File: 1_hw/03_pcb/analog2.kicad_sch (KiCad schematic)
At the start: 17 parts

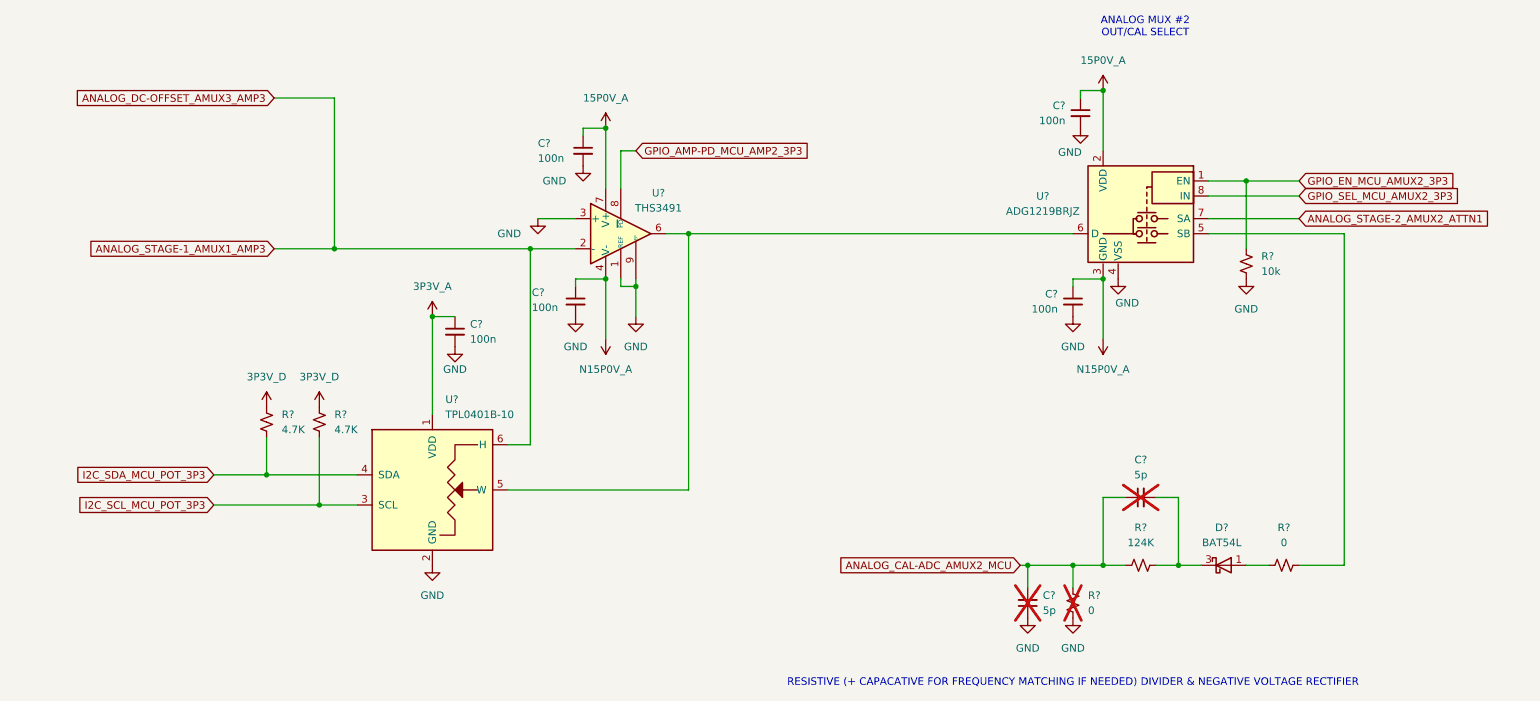
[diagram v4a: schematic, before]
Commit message: FEAT: Added Clocking Sheet, FPGA Flash, and FPGA Decoupling.
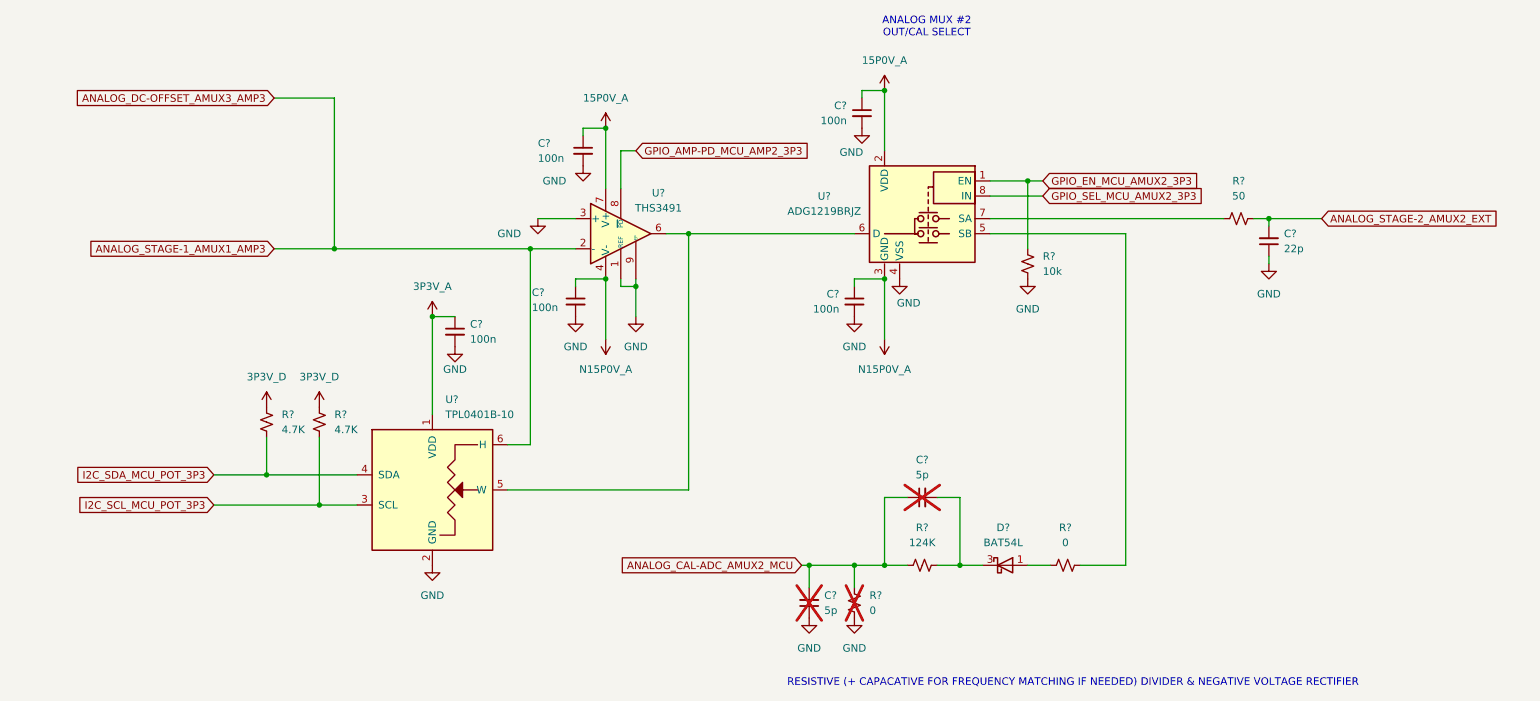
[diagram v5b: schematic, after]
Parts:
- added C?: 22p, symbol Device:C_Small
- added R?: 50, symbol Device:R_Small_US
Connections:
- net GND: now also C?.1
- net ANALOG_STAGE-2_AMUX2_ATTN1: no longer names the net of U?.7 (SA)
- net ANALOG_STAGE-2_AMUX2_ATTN1: now also R?.2
- new net ANALOG_STAGE-2_AMUX2_EXT: C?.2, R?.1
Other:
- moved on the sheet: C?, D?, R?, U?

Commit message: FEAT: Added Connectors on Schematic. Created Connector Footprints.
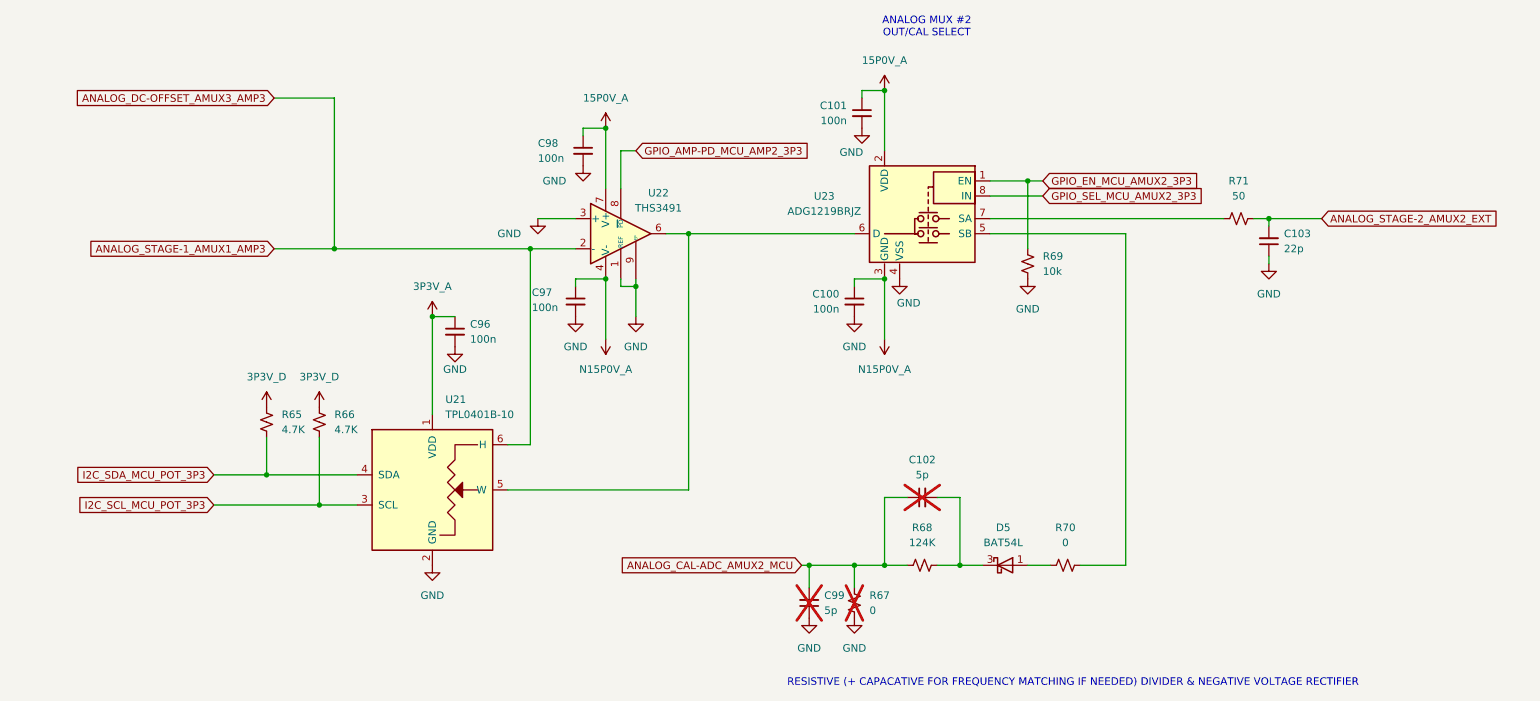
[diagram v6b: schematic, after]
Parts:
- gave numbers to parts that had none: 19
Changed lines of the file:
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@@
 		(dnp no)
 		(fields_autoplaced yes)
-		(property "Reference" "U?"
+		(property "Reference" "U21"
 			(at 83.4741 111.76 0)
 			(effects
@@
 			(project ""
 				(path "/866ef9be-3b01-4288-a6e0-a2357aa17e50/e46c6640-71a3-4b78-b602-0f6be9676e36"
-					(reference "U?")
+					(reference "U21")
 					(unit 1)
 				)
@@
 		(dnp yes)
 		(fields_autoplaced yes)
-		(property "Reference" "R?"
+		(property "Reference" "R67"
 			(at 154.94 144.7799 0)
 			(effects
@@
 			(project "arb"
 				(path "/866ef9be-3b01-4288-a6e0-a2357aa17e50/e46c6640-71a3-4b78-b602-0f6be9676e36"
-					(reference "R?")
+					(reference "R67")
 					(unit 1)
 				)
@@
 		(dnp no)
 		(fields_autoplaced yes)
-		(property "Reference" "R?"
+		(property "Reference" "R69"
 			(at 184.15 87.6299 0)
 			(effects
@@
 			(project "arb"
 				(path "/866ef9be-3b01-4288-a6e0-a2357aa17e50/e46c6640-71a3-4b78-b602-0f6be9676e36"
-					(reference "R?")
+					(reference "R69")
 					(unit 1)
 				)
@@
 		(dnp no)
 		(fields_autoplaced yes)
-		(property "Reference" "C?"
+		(property "Reference" "C101"
 			(at 151.13 62.2363 0)
 			(effects
@@
 			(project "arb"
 				(path "/866ef9be-3b01-4288-a6e0-a2357aa17e50/e46c6640-71a3-4b78-b602-0f6be9676e36"
-					(reference "C?")
+					(reference "C101")
 					(unit 1)
 				)
@@
 		(dnp yes)
 		(fields_autoplaced yes)
-		(property "Reference" "C?"
+		(property "Reference" "C99"
 			(at 147.32 144.7735 0)
 			(effects
@@
 			(project "arb"
 				(path "/866ef9be-3b01-4288-a6e0-a2357aa17e50/e46c6640-71a3-4b78-b602-0f6be9676e36"
-					(reference "C?")
+					(reference "C99")
 					(unit 1)
 				)
@@
 		(on_board yes)
 		(dnp no)
-		(property "Reference" "U?"
+		(property "Reference" "U22"
 			(at 119.38 76.962 0)
 			(effects
@@
 			(project ""
 				(path "/866ef9be-3b01-4288-a6e0-a2357aa17e50/e46c6640-71a3-4b78-b602-0f6be9676e36"
-					(reference "U?")
+					(reference "U22")
 					(unit 1)
 				)
@@
 		(on_board yes)
 		(dnp no)
-		(property "Reference" "C?"
+		(property "Reference" "C98"
 			(at 99.06 68.58 0)
 			(effects
@@
 			(project "arb"
 				(path "/866ef9be-3b01-4288-a6e0-a2357aa17e50/e46c6640-71a3-4b78-b602-0f6be9676e36"
-					(reference "C?")
+					(reference "C98")
 					(unit 1)
 				)
@@
 		(dnp no)
 		(fields_autoplaced yes)
-		(property "Reference" "C?"
+		(property "Reference" "C100"
 			(at 149.86 93.9863 0)
 			(effects
@@
 			(project "arb"
 				(path "/866ef9be-3b01-4288-a6e0-a2357aa17e50/e46c6640-71a3-4b78-b602-0f6be9676e36"
-					(reference "C?")
+					(reference "C100")
 					(unit 1)
 				)
@@
 		(dnp no)
 		(fields_autoplaced yes)
-		(property "Reference" "R?"
+		(property "Reference" "R68"
 			(at 163.83 133.35 90)
 			(effects
@@
 			(project "arb"
 				(path "/866ef9be-3b01-4288-a6e0-a2357aa17e50/e46c6640-71a3-4b78-b602-0f6be9676e36"
-					(reference "R?")
+					(reference "R68")
 					(unit 1)
 				)
@@
 		(on_board yes)
 		(dnp no)
-		(property "Reference" "C?"
+		(property "Reference" "C97"
 			(at 98.044 93.726 0)
 			(effects
@@
 			(project "arb"
 				(path "/866ef9be-3b01-4288-a6e0-a2357aa17e50/e46c6640-71a3-4b78-b602-0f6be9676e36"
-					(reference "C?")
+					(reference "C97")
 					(unit 1)
 				)
@@
 		(dnp no)
 		(fields_autoplaced yes)
-		(property "Reference" "R?"
+		(property "Reference" "R70"
 			(at 187.96 133.35 90)
 			(effects
@@
 			(project "arb"
 				(path "/866ef9be-3b01-4288-a6e0-a2357aa17e50/e46c6640-71a3-4b78-b602-0f6be9676e36"
-					(reference "R?")
+					(reference "R70")
 					(unit 1)
 				)
@@
 		(dnp no)
 		(fields_autoplaced yes)
-		(property "Reference" "R?"
+		(property "Reference" "R66"
 			(at 64.77 114.2999 0)
 			(effects
@@
 			(project "arb"
 				(path "/866ef9be-3b01-4288-a6e0-a2357aa17e50/e46c6640-71a3-4b78-b602-0f6be9676e36"
-					(reference "R?")
+					(reference "R66")
 					(unit 1)
 				)
@@
 		(dnp yes)
 		(fields_autoplaced yes)
-		(property "Reference" "C?"
+		(property "Reference" "C102"
 			(at 163.8363 121.92 90)
 			(effects
@@
 			(project "arb"
 				(path "/866ef9be-3b01-4288-a6e0-a2357aa17e50/e46c6640-71a3-4b78-b602-0f6be9676e36"
-					(reference "C?")
+					(reference "C102")
 					(unit 1)
 				)
@@
 		(dnp no)
 		(fields_autoplaced yes)
-		(property "Reference" "R?"
+		(property "Reference" "R71"
 			(at 217.17 74.93 90)
 			(effects
@@
 			(project "arb"
 				(path "/866ef9be-3b01-4288-a6e0-a2357aa17e50/e46c6640-71a3-4b78-b602-0f6be9676e36"
-					(reference "R?")
+					(reference "R71")
 					(unit 1)
 				)
@@
 		(dnp no)
 		(fields_autoplaced yes)
-		(property "Reference" "D?"
+		(property "Reference" "D5"
 			(at 177.4825 133.35 0)
 			(effects
@@
 			(project "arb"
 				(path "/866ef9be-3b01-4288-a6e0-a2357aa17e50/e46c6640-71a3-4b78-b602-0f6be9676e36"
-					(reference "D?")
+					(reference "D5")
 					(unit 1)
 				)
@@
 		(dnp no)
 		(fields_autoplaced yes)
-		(property "Reference" "C?"
+		(property "Reference" "C96"
 			(at 87.63 99.0663 0)
 			(effects
@@
 			(project "arb"
 				(path "/866ef9be-3b01-4288-a6e0-a2357aa17e50/e46c6640-71a3-4b78-b602-0f6be9676e36"
-					(reference "C?")
+					(reference "C96")
 					(unit 1)
 				)
@@
 		(dnp no)
 		(fields_autoplaced yes)
-		(property "Reference" "R?"
+		(property "Reference" "R65"
 			(at 55.88 114.2999 0)
 			(effects
@@
 			(project "arb"
 				(path "/866ef9be-3b01-4288-a6e0-a2357aa17e50/e46c6640-71a3-4b78-b602-0f6be9676e36"
-					(reference "R?")
+					(reference "R65")
 					(unit 1)
 				)
@@
 		(dnp no)
 		(fields_autoplaced yes)
-		(property "Reference" "U?"
+		(property "Reference" "U23"
 			(at 147.32 77.5014 0)
 			(effects
@@
 			(project ""
 				(path "/866ef9be-3b01-4288-a6e0-a2357aa17e50/e46c6640-71a3-4b78-b602-0f6be9676e36"
-					(reference "U?")
+					(reference "U23")
 					(unit 1)
 				)
@@
 		(dnp no)
 		(fields_autoplaced yes)
-		(property "Reference" "C?"
+		(property "Reference" "C103"
 			(at 224.79 83.8135 0)
 			(effects
@@
 			(project "arb"
 				(path "/866ef9be-3b01-4288-a6e0-a2357aa17e50/e46c6640-71a3-4b78-b602-0f6be9676e36"
-					(reference "C?")
-					(unit 1)
-				)
+					(reference "C103")
+					(unit 1)
+				)

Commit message: FEAT: Assigned Reference Designators; Assigned Passives Part Numbers & Footprints (0603); Assigned LCSC P/Ns.
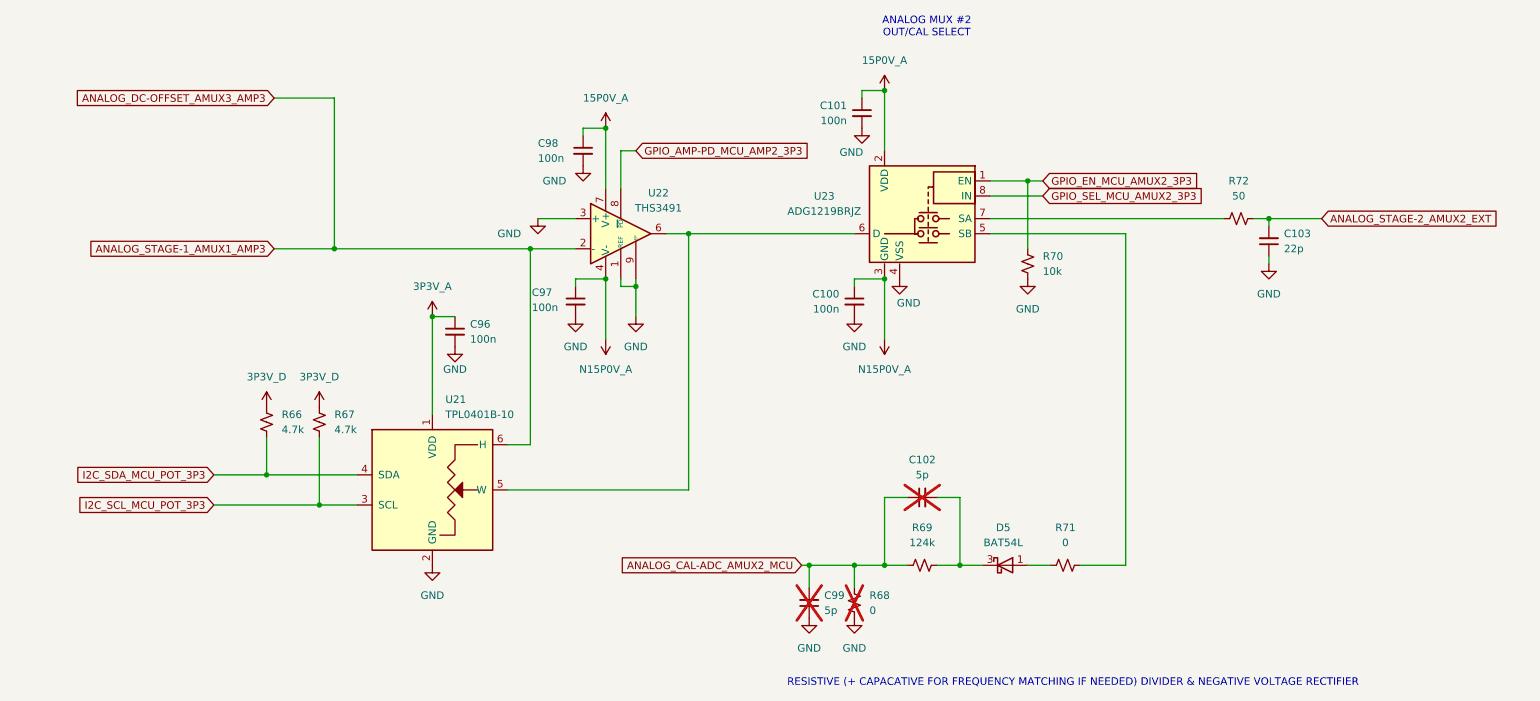
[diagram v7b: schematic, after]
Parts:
- C100, C101, C96, C97, C98: LCSC (none) -> C24452; PN CL10B104JB8NNNC -> (none); Part Number (none) -> CL10B104JB8NNNC
- C102, C99: footprint (none) -> Capacitor_SMD:C_0603_1608Metric; LCSC (none) -> C327203; Part Number (none) -> CC0603CRNPO9BN5R0
- C103: footprint (none) -> Capacitor_SMD:C_0603_1608Metric; LCSC (none) -> C1653; Part Number (none) -> CL10C220JB8NNNC
- D5: LCSC (none) -> C94399
- R66: renamed from R65; value 4.7K -> 4.7k; footprint (none) -> Resistor_SMD:R_0603_1608Metric; LCSC (none) -> C99782; Part Number (none) -> RC0603FR-074K7L
- R67: renamed from R66; value 4.7K -> 4.7k; footprint (none) -> Resistor_SMD:R_0603_1608Metric; LCSC (none) -> C99782; Part Number (none) -> RC0603FR-074K7L
- R68: renamed from R67; footprint (none) -> Resistor_SMD:R_0603_1608Metric; LCSC (none) -> C15402; Part Number (none) -> 0603WAJ0000T5E
- R69: renamed from R68; value 124K -> 124k; footprint (none) -> Resistor_SMD:R_0603_1608Metric; LCSC (none) -> C22788; Part Number (none) -> 0603WAF1243T5E
- R70: renamed from R69; LCSC (none) -> C25804; PN CR-03FC7---10K -> (none); Part Number (none) -> 0603WAF1002T5E
- R71: renamed from R70; footprint (none) -> Resistor_SMD:R_0603_1608Metric; LCSC (none) -> C15402; Part Number (none) -> 0603WAJ0000T5E
- R72: renamed from R71; footprint (none) -> Resistor_SMD:R_0603_1608Metric; LCSC (none) -> C849792; Part Number (none) -> RT0603BRE0750RL
- U21: LCSC (none) -> C2666599
- U22: LCSC (none) -> C2058693
- U23: footprint BRZK_TBD -> (none); LCSC (none) -> C579007

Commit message: FEAT: Added MCU Flash. Finished creating & assigning footprints. Ran ERC & cleared out issues. Ready for Layout.
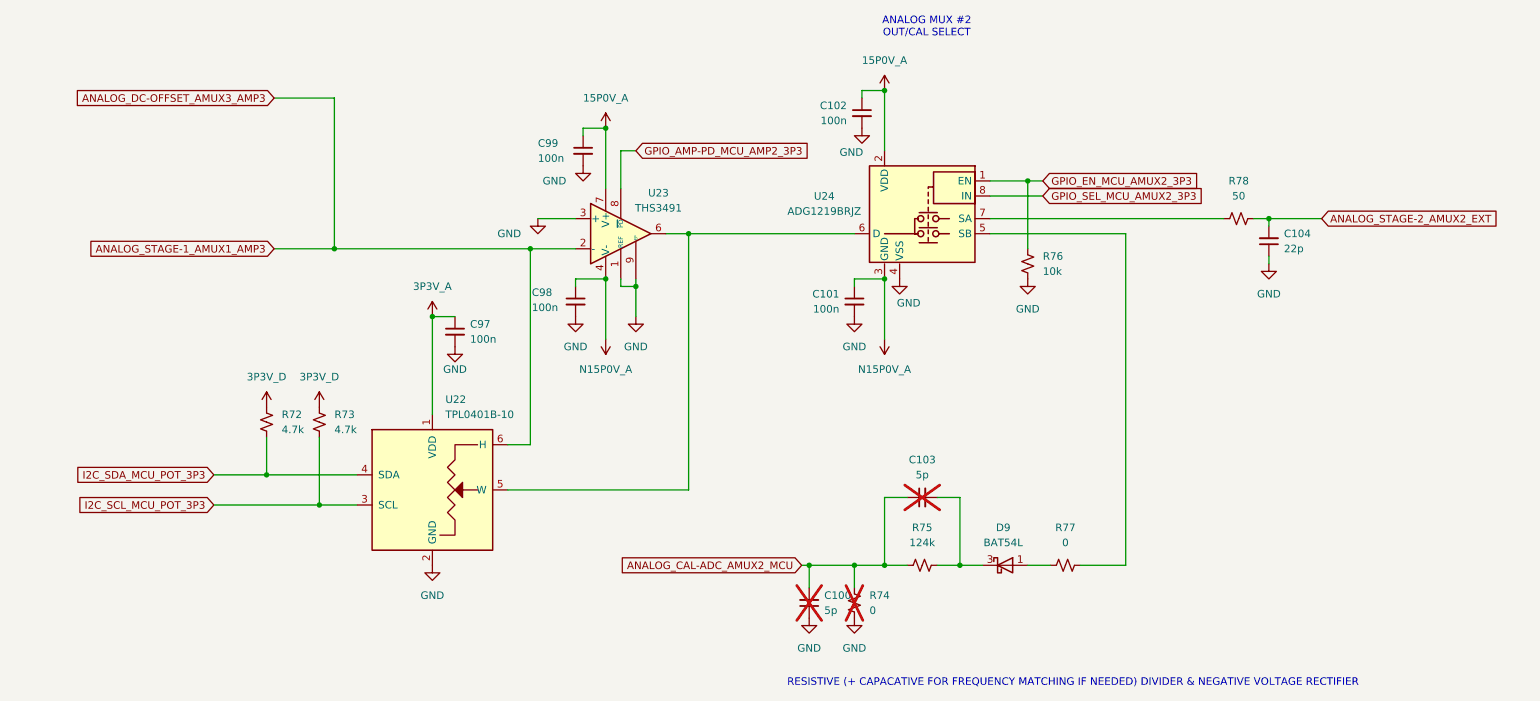
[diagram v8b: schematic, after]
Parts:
- U24: renamed from U23; footprint (none) -> Package_TO_SOT_SMD:SOT-23-8
- renumbered C99 to C100, C100 to C101, C101 to C102, C102 to C103, C103 to C104, C96 to C97, C97 to C98, C98 to C99, D5 to D9, R66 to R72, R67 to R73, R68 to R74, R69 to R75, R70 to R76, R71 to R77, R72 to R78, U21 to U22, U22 to U23
